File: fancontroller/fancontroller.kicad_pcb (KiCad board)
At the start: 2 copper layers, 60 x 60 mm, 25 parts, among them J1 Power, J2 Serial Conn, M1 FAN0, M2 FAN0, M3 FAN0, M4 FAN0, M5 FAN0, M6 FAN0, SW1 SW_Push, U2 ESP32-WROOM-32, U3 AMS1117-3.3

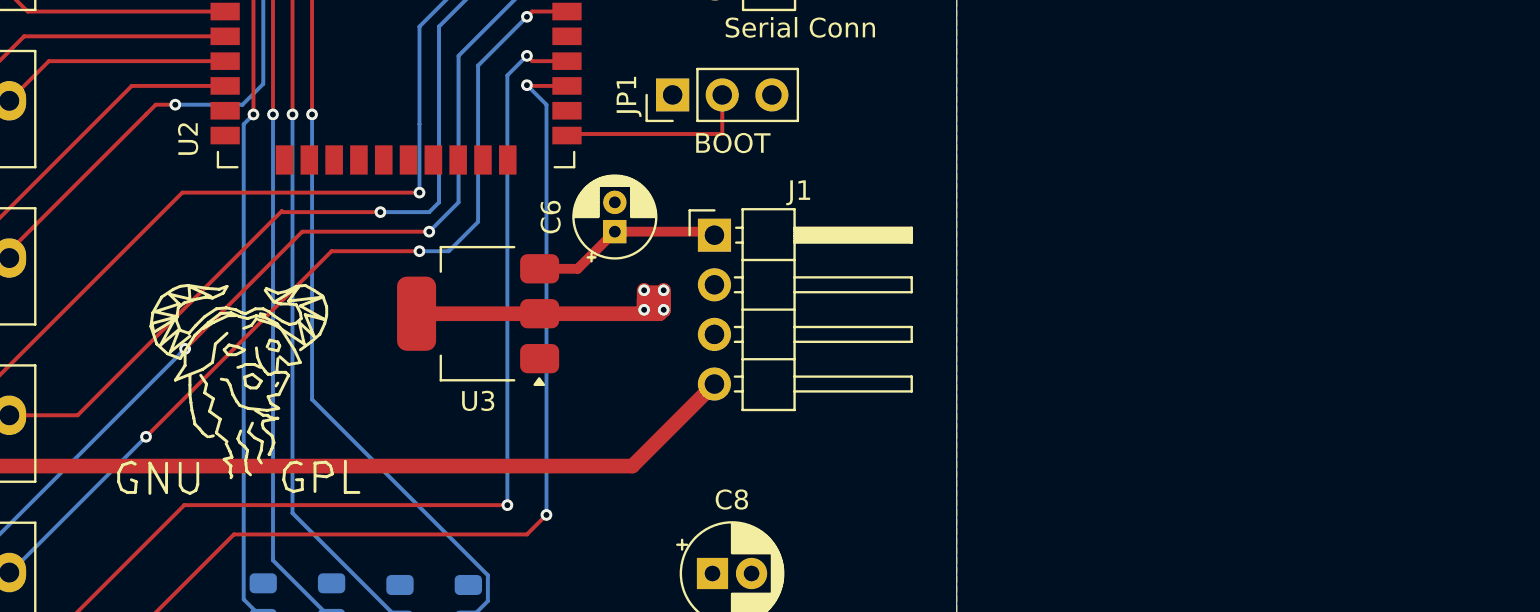
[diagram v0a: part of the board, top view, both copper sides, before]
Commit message: CMOS treiber für PWM output hinzugefügt, sicher ist sicher und extern pullup widerstände für Tacho inputs. Die sollten alle Teile für den ersten Prototypen sein.
PCB Layout muss angepasst werden und neu geroutet werden. Danach ready für ersten prototypen :)
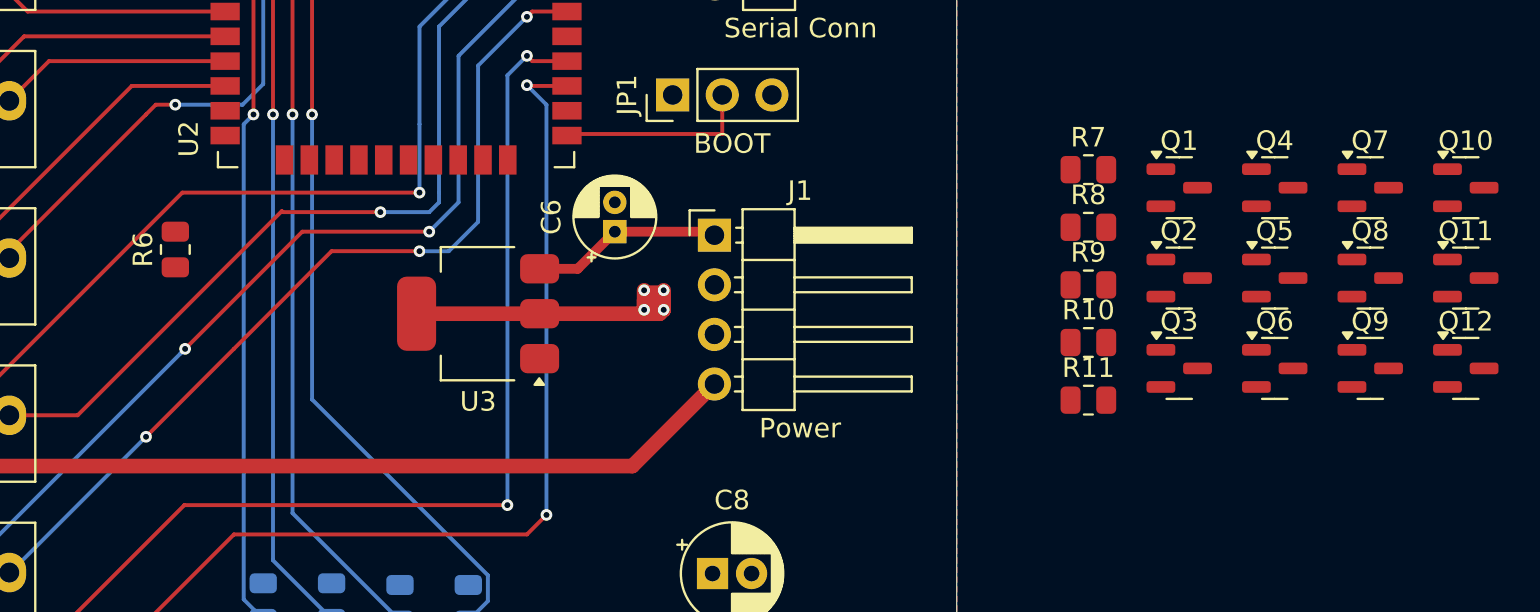
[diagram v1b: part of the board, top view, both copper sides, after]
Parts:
- removed REF**: Symbol_GNU-Logo_SilkscreenTop, Symbol:Symbol_GNU-Logo_SilkscreenTop
- added Q1: AO3400A, Package_TO_SOT_SMD:SOT-23, F.Cu at (171.4, 88.2)
- added Q10: AO3401A, Package_TO_SOT_SMD:SOT-23, F.Cu at (186.1, 88.2)
- added Q11: AO3400A, Package_TO_SOT_SMD:SOT-23, F.Cu at (186.1, 92.9)
- added Q12: AO3401A, Package_TO_SOT_SMD:SOT-23, F.Cu at (186.1, 97.5)
- added Q2: AO3401A, Package_TO_SOT_SMD:SOT-23, F.Cu at (171.4, 92.9)
- added Q3: AO3400A, Package_TO_SOT_SMD:SOT-23, F.Cu at (171.4, 97.5)
- added Q4: AO3401A, Package_TO_SOT_SMD:SOT-23, F.Cu at (176.3, 88.2)
- added Q5: AO3400A, Package_TO_SOT_SMD:SOT-23, F.Cu at (176.3, 92.9)
- added Q6: AO3401A, Package_TO_SOT_SMD:SOT-23, F.Cu at (176.3, 97.5)
- added Q7: AO3400A, Package_TO_SOT_SMD:SOT-23, F.Cu at (181.2, 88.2)
- added Q8: AO3401A, Package_TO_SOT_SMD:SOT-23, F.Cu at (181.2, 92.9)
- added Q9: AO3400A, Package_TO_SOT_SMD:SOT-23, F.Cu at (181.2, 97.5)
- added R10: R, Resistor_SMD:R_0805_2012Metric, F.Cu at (166.7, 96.2)
- added R11: R, Resistor_SMD:R_0805_2012Metric, F.Cu at (166.7, 99.1)
- added R6: R, Resistor_SMD:R_0805_2012Metric, F.Cu at (120.0, 91.4)
- added R7: R, Resistor_SMD:R_0805_2012Metric, F.Cu at (166.7, 87.3)
- added R8: R, Resistor_SMD:R_0805_2012Metric, F.Cu at (166.7, 90.3)
- added R9: R, Resistor_SMD:R_0805_2012Metric, F.Cu at (166.7, 93.2)
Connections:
- M1 pad 4: PWM0 -> Net-(M1-PWM)
- M2 pad 4: PWM1 -> Net-(M2-PWM)
- M3 pad 4: PWM2 -> Net-(M3-PWM)
- M4 pad 4: PWM3 -> Net-(M4-PWM)
- M5 pad 4: PWM4 -> Net-(M5-PWM)
- M6 pad 4: PWM5 -> Net-(M6-PWM)

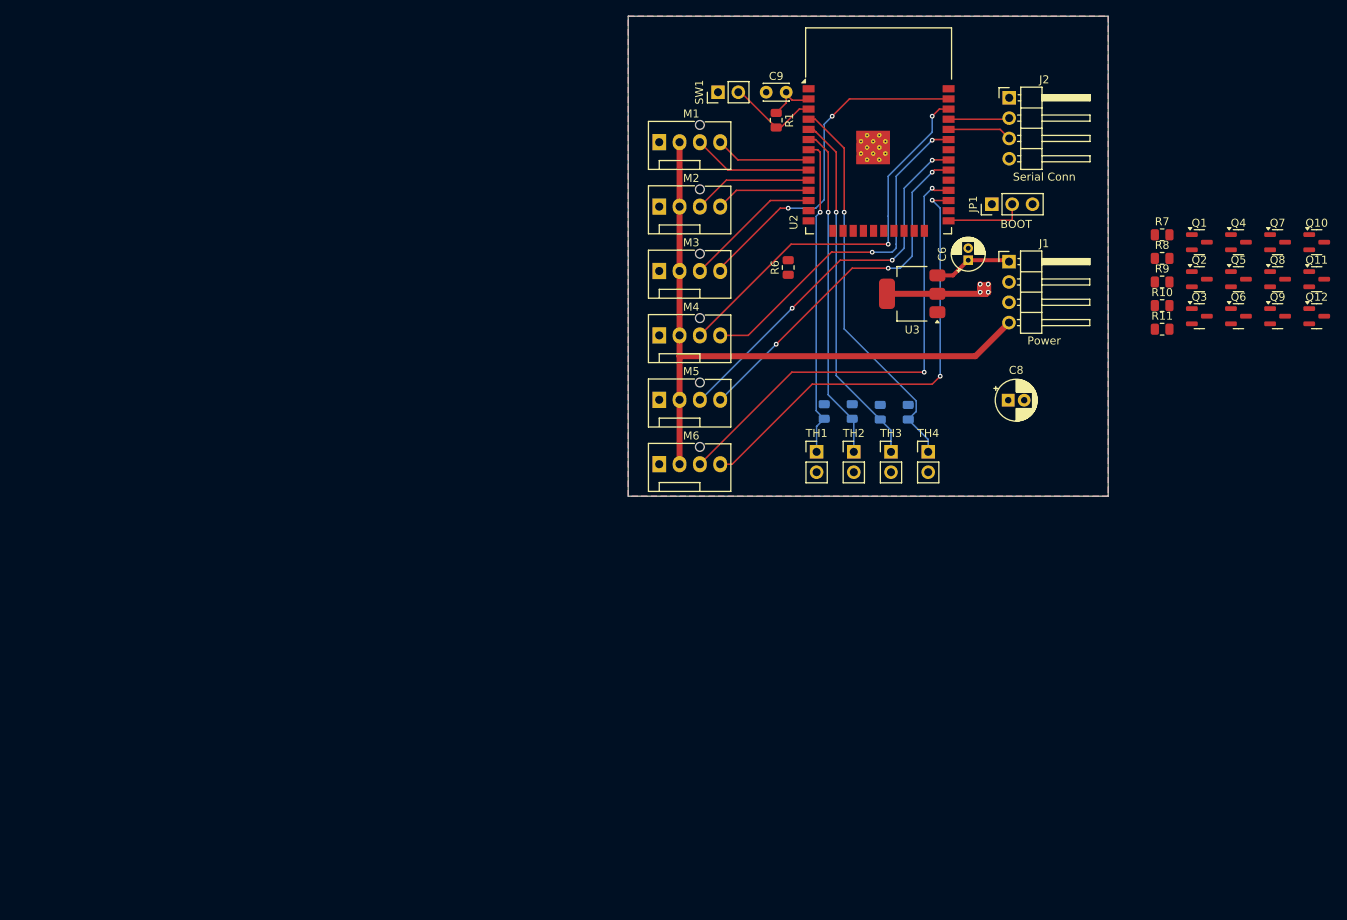
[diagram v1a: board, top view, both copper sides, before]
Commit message: Routing für ersten prototypen fertig und erste Teilnummern Parts zugeordnet für assembly preview
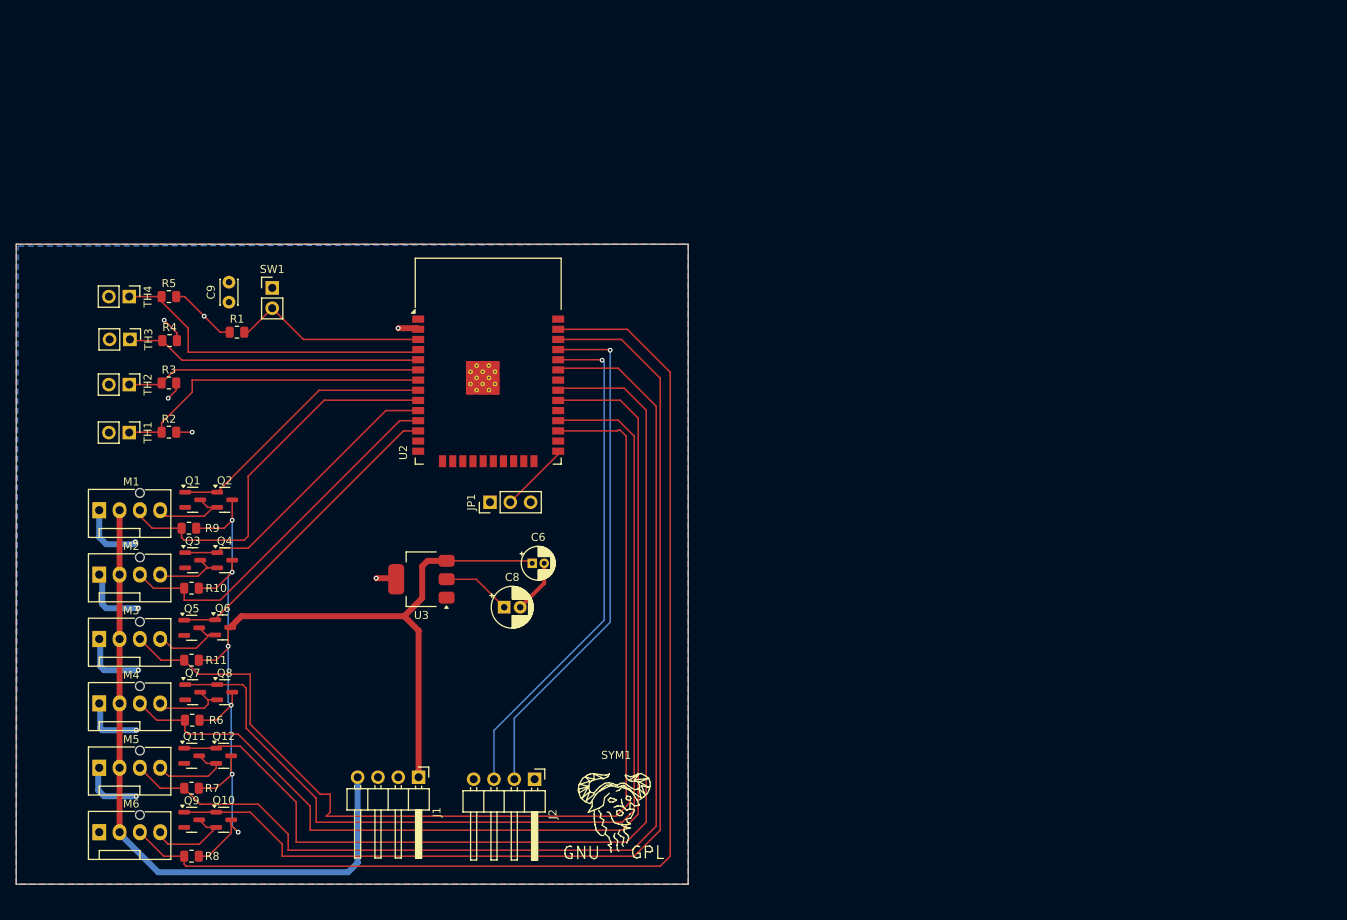
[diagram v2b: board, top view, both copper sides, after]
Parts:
- added SYM1: SYM_EasterEgg_42x60mm, Symbol:Symbol_GNU-Logo_SilkscreenTop, F.Cu at (98.5, 158.4)
- R10, R11, R6, R7, R8, R9: value R -> 10k
- R2, R3, R4, R5: moved to F.Cu
- moved Q10 154.5 mm to (49.4, 160.4)
- moved Q11 152.7 mm to (45.4, 152.4)
- moved Q9 149.6 mm to (45.4, 160.4)
- moved Q12 147.3 mm to (49.4, 152.4)
- moved Q7 146.8 mm to (45.6, 144.5)
- moved R8 142.5 mm to (45.4, 165.0), turned to 180 degrees
- moved Q8 141.4 mm to (49.6, 144.5)
- moved R7 139.7 mm to (45.4, 156.5), turned to 180 degrees
- moved Q5 137.9 mm to (45.4, 136.4)
- moved Q4 132.8 mm to (49.6, 128.0)
- moved Q6 132.8 mm to (49.3, 136.4)
- moved Q1 129.9 mm to (45.6, 120.5)
- moved Q3 129.5 mm to (45.6, 128.0)
- moved R11 128.2 mm to (45.4, 140.5), turned to 180 degrees
- moved R10 126.4 mm to (45.4, 131.5), turned to 180 degrees
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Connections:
- U2 pad 10: Tacho1 -> PWM1
- U2 pad 11: PWM1 -> Tacho1
- U2 pad 12: Tacho2 -> PWM2
- U2 pad 27: PWM5 -> Tacho2
- U2 pad 28: Tacho5 -> PWM3
- U2 pad 30: PWM4 -> Tacho3
- U2 pad 31: Tacho4 -> PWM4
- U2 pad 33: PWM3 -> Tacho4
- U2 pad 36: Tacho3 -> PWM5
- U2 pad 37: PWM2 -> Tacho5
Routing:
- net +5V: track 9.81 -> 147.7 mm, vias 0 -> 6
- net Tacho2: track 17.2 -> 132.0 mm
- net Tacho4: track 48.3 -> 138.0 mm, vias 3 -> 0
- net Tacho5: track 58.4 -> 145.9 mm, vias 2 -> 0
- net PWM4: track 45.1 -> 130.5 mm, vias 3 -> 0
- net Tacho3: track 49.0 -> 132.7 mm, vias 2 -> 0
- net PWM3: track 44.4 -> 125.7 mm, vias 2 -> 0
- net PWM5: track 56.5 -> 135.3 mm, vias 2 -> 0
- net TX: track 7.63 -> 65.1 mm, vias 0 -> 1
- net RX: track 8.04 -> 63.7 mm, vias 0 -> 1
- net GND: track 0.00 -> 47.7 mm, vias 0 -> 5
- net Tacho0: track 15.0 -> 49.1 mm
- net Tacho1: track 15.0 -> 46.3 mm
- net PWM1: track 11.9 -> 36.5 mm
- net PWM0: track 12.0 -> 34.4 mm
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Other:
- board size 60 x 60 mm -> 84 x 80 mm

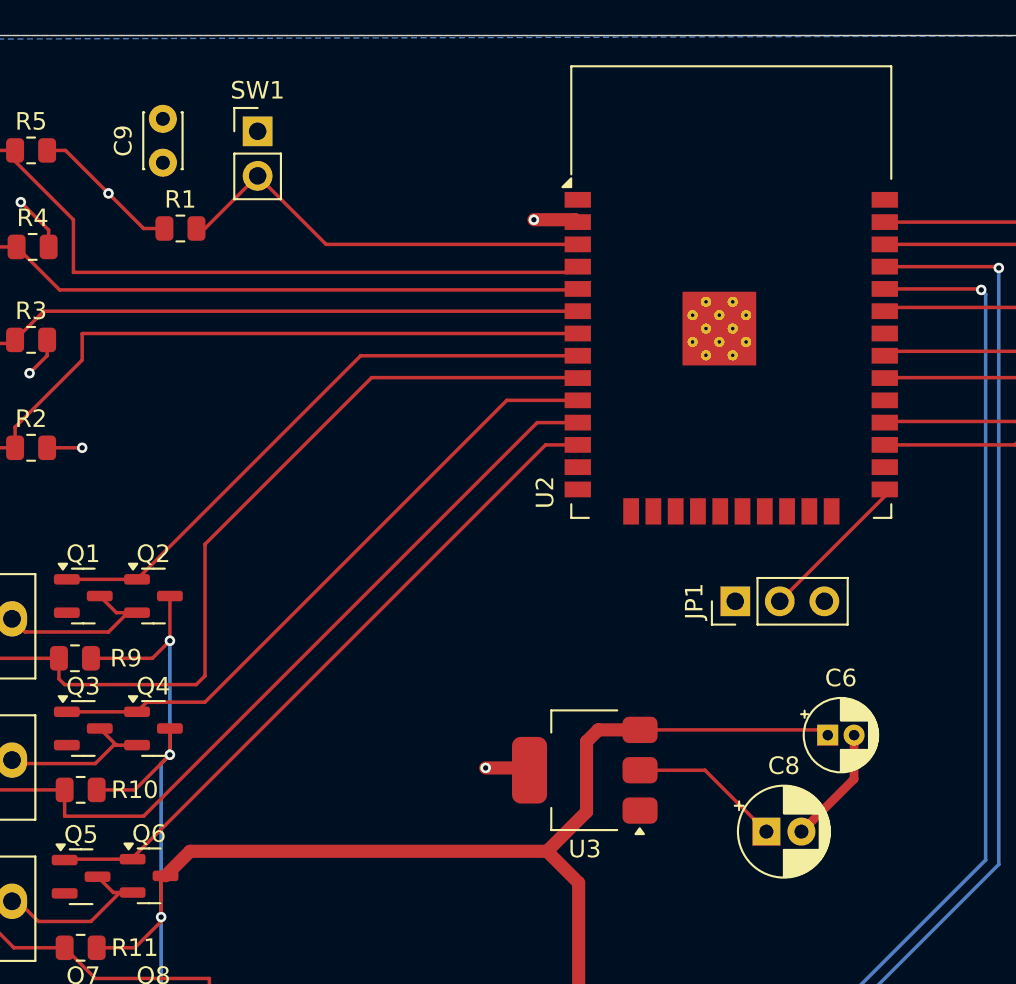
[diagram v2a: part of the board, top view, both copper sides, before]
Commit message: JLCPCB order rotations fixed for most parts
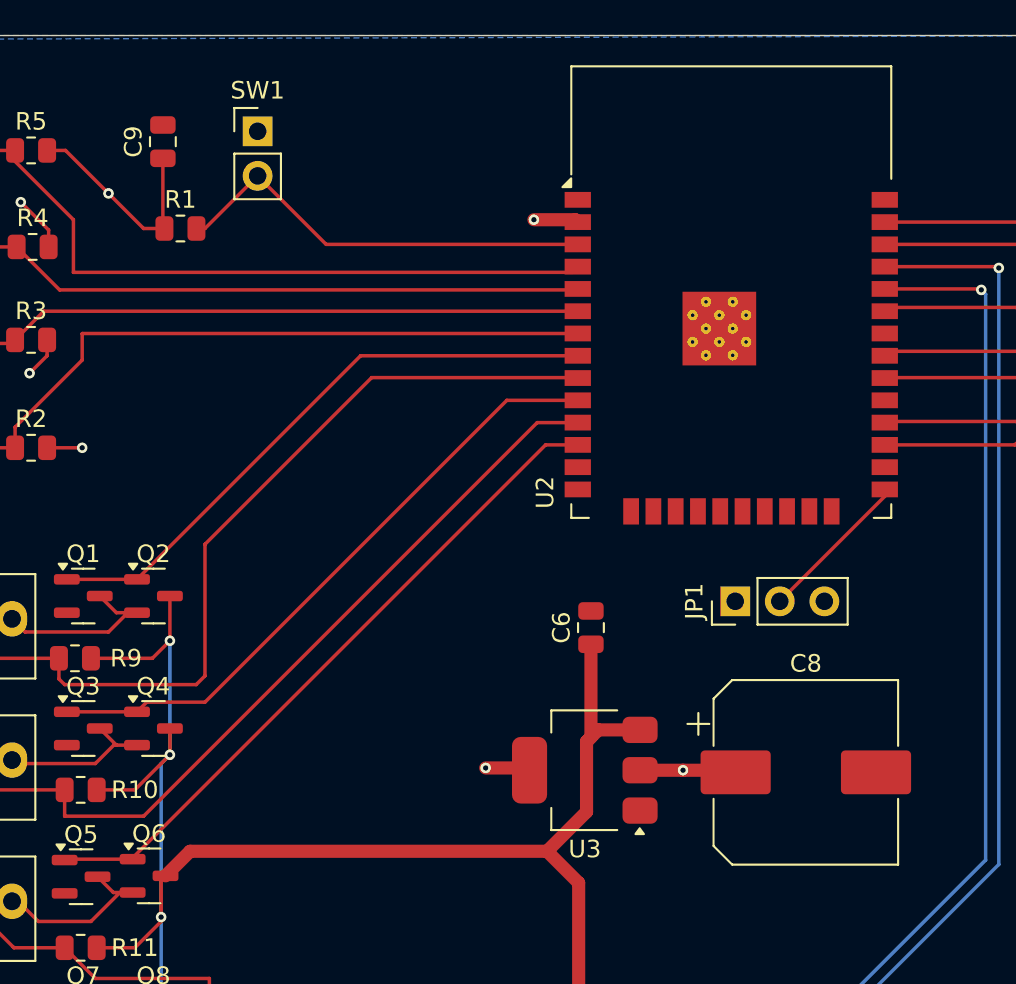
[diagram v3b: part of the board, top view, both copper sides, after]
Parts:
- C6: footprint Capacitor_THT:CP_Radial_D4.0mm_P1.50mm -> Capacitor_SMD:C_0805_2012Metric
- C8: footprint Capacitor_THT:CP_Radial_D5.0mm_P2.00mm -> Capacitor_SMD:CP_Elec_10x10
- C9: footprint Capacitor_THT:C_Disc_D3.0mm_W2.0mm_P2.50mm -> Capacitor_SMD:C_0805_2012Metric
- moved C6 14.8 mm to (74.5, 122.2), turned to 90 degrees
- moved C8 4.06 mm to (86.8, 130.5)
- moved C9 1.20 mm to (50.1, 94.5)
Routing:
- net GND: track 47.7 -> 41.0 mm
- net +5V: track 147.7 -> 142.5 mm
- net +3.3V: track 29.8 -> 30.7 mm, vias 6 -> 7

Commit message: prepare to start dev on v1.2
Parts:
- removed SYM1: SYM_EasterEgg_42x60mm, Symbol:Symbol_GNU-Logo_SilkscreenTop
- added REF**: Symbol_GNU-Logo_SilkscreenTop, Symbol:Symbol_GNU-Logo_SilkscreenTop, F.Cu at (99.5, 157.5)
